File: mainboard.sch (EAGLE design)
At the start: 140 parts, among them J1 503182-1852, J2 10118194-0001LF, J3 DCJ0303, Q1 IRLML2803, Q10 IRLML5103, Q11 IRLML5103, Q12 IRLML5103, Q13 IRLML5103, Q14 IRLML2803, Q15 IRLML2803, Q16 IRLML5103, Q2 IRLML2803, Q5 IRLML2803, Q6 IRLML2803, Q7 IRLML2803, Q8 IRLML2803, Q9 IRLML5103, U1 MAX706R, U12 EP2W+, U13 RFM23BP, U14 S1216V8, U15 XTB_2018_07_15, U16 XTB_2018_07_15, U17 XTB_2018_07_15, U18 XTB_2018_07_15, U2 FXAS21002FXAS21002, U20 MR25H40MDF, U3 LSM9DS1, U4 ATSAMD21G-A, U5 MAX4372TEUK+T, U6 LTC4121-4.2, U7 TPS54226PWPRPWP14_2P31X2P46-L, U8 PE014006, U9 PE014006, X1 BU-SMA-V, X2 BU-SMA-V, X3 BU-SMA-V, Y1 32.768kHz

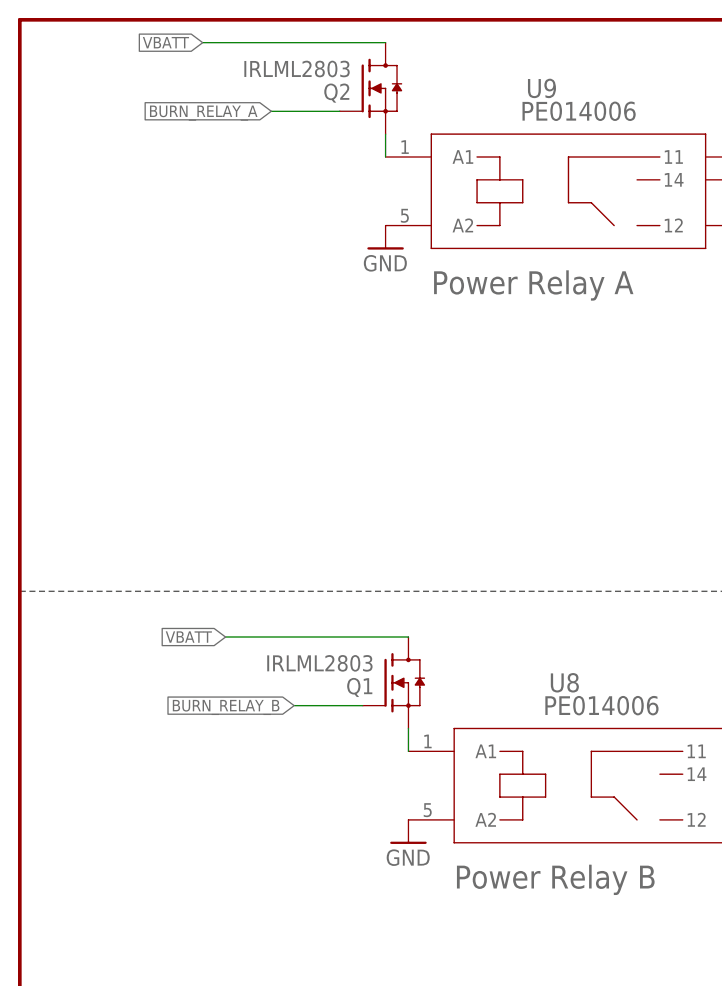
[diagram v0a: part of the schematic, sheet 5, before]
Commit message: updated mainboard to KMB-23
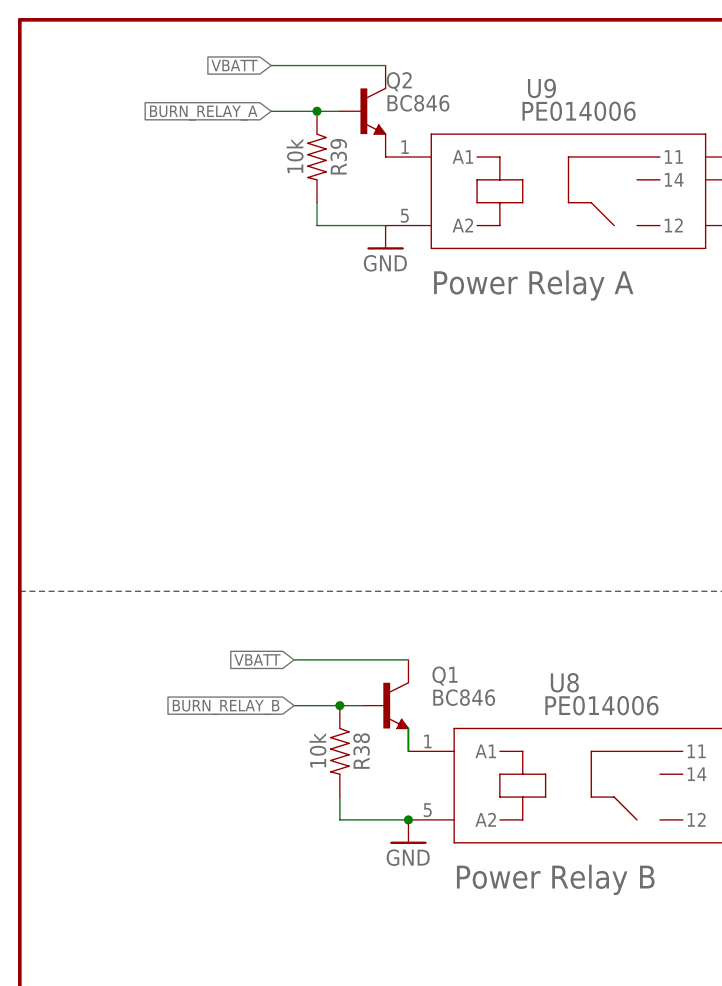
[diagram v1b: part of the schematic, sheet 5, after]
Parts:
- added R38, R39: 10k, SparkFun-Resistors:RESISTOR0603
- added R40: 2.1M, resistor:R-US_R0603
- added R41: 845K, resistor:R-US_R0603
- added R42: 10k, resistor:R-US_R0603
- C20: value 2.2nF -> 22nF
- Q1, Q2: value IRLML2803 -> BC846; device maholli:IRLML2803TRPBF -> transistor:BC846
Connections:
- new net GND4: R39.2
- new net N$31: R40.2, R41.2, U6.BATSNS
- new net N$49: U13.GPIO_0, U13.RXON
- new net N$54: R41.1, U6.NC
- new net N$55: U13.GPIO_1, U13.TXON
- net 3.3V: now also U18.QFN18, U2.SA0/MISO
- net BURN_RELAY_A: now also Q2.B, R39.1; no longer Q2.G
- net BURN_RELAY_B: now also Q1.B, R38.1; no longer Q1.G
- net GND: now also R38.2, R42.1, U18.QFN4; no longer U6.NC
- net LION1: now also R40.1; no longer U6.BATSNS
- net N$38: now also Q2.E; no longer Q2.S
- net N$40: now also Q1.E; no longer Q1.S
- net N$8: now also U1.!MR
- net UART1_RX: now also U4.PB09(AIN3/SER4:1/TC4:1); no longer U4.PB08(AIN2/SER4:0/TC4:0)
- net UART1_TX: now also U4.PB08(AIN2/SER4:0/TC4:0); no longer U4.PB09(AIN3/SER4:1/TC4:1)
- net VBATT: now also Q1.C, Q2.C; no longer Q1.D, Q2.D
- net WDT_WDI: now also R42.2
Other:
- moved on the sheet: C19, F1
